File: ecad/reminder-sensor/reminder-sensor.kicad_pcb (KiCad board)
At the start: 2 copper layers, 8.3 x 25.4 mm, 5 parts, among them J1 0530470310, U1 QRD1113GR

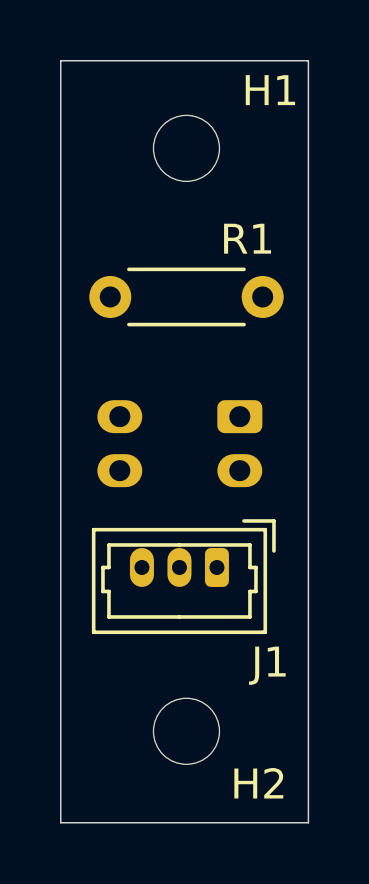
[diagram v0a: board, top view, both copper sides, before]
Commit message: Finished routing, silkscreen details.
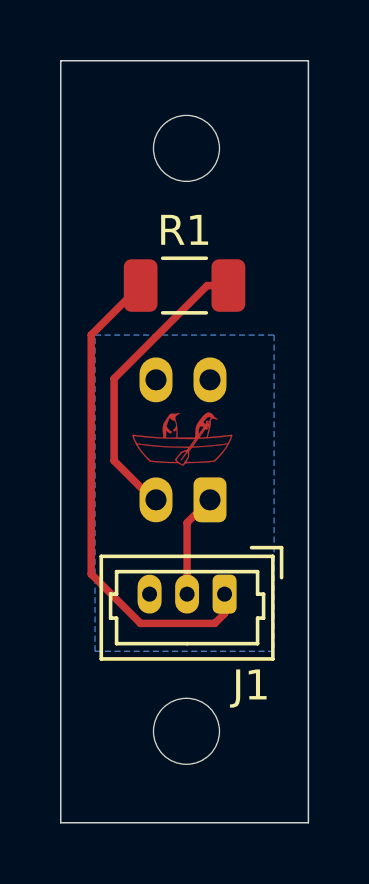
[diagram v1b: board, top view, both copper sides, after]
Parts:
- added G***: LOGO, Decals:tiny-penguin, F.Cu at (183.1, 88.8)
- R1: footprint Resistor_THT:R_Axial_DIN0204_L3.6mm_D1.6mm_P5.08mm_Horizontal -> Resistor_SMD:R_1206_3216Metric
- moved U1 2.95 mm to (184.0, 90.8), turned to 180 degrees
- moved R1 2.50 mm to (183.2, 83.7)
- moved J1 0.92 mm to (184.5, 94.0)
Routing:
- net +5V: track 0.00 -> 16.2 mm
- net Net-(R1-Pad2): track 0.00 -> 9.77 mm
- net /OUTPUT: track 0.00 -> 3.46 mm
- added copper zone on B.Cu, net GND
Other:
- board text added: "5.3.21"
- board text added: "JDG"
- board text added: "med-reminder sensor revA"

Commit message: Added rev text and chamfered corners of PCB
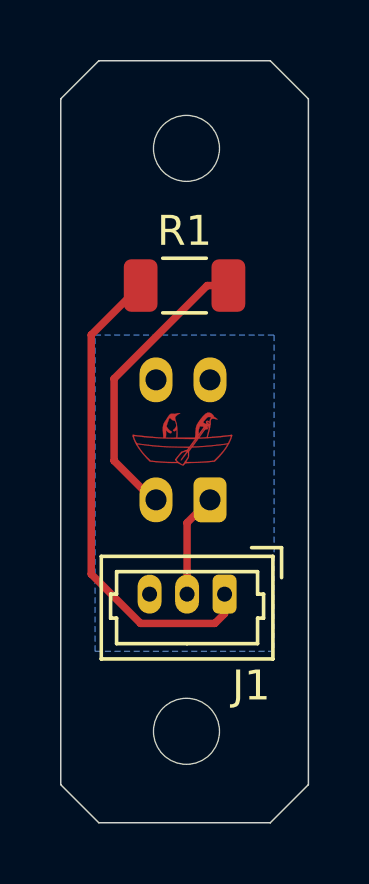
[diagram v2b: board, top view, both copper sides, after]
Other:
- outline, holes or cut-outs redrawn
